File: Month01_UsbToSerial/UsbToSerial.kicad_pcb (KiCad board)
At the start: 2 copper layers, 36.8 x 24.1 mm, 14 parts, among them J1 USB_B_Micro, J2 Conn_01x07_Female, J3 Conn_01x07_Female, U1 FT232RL

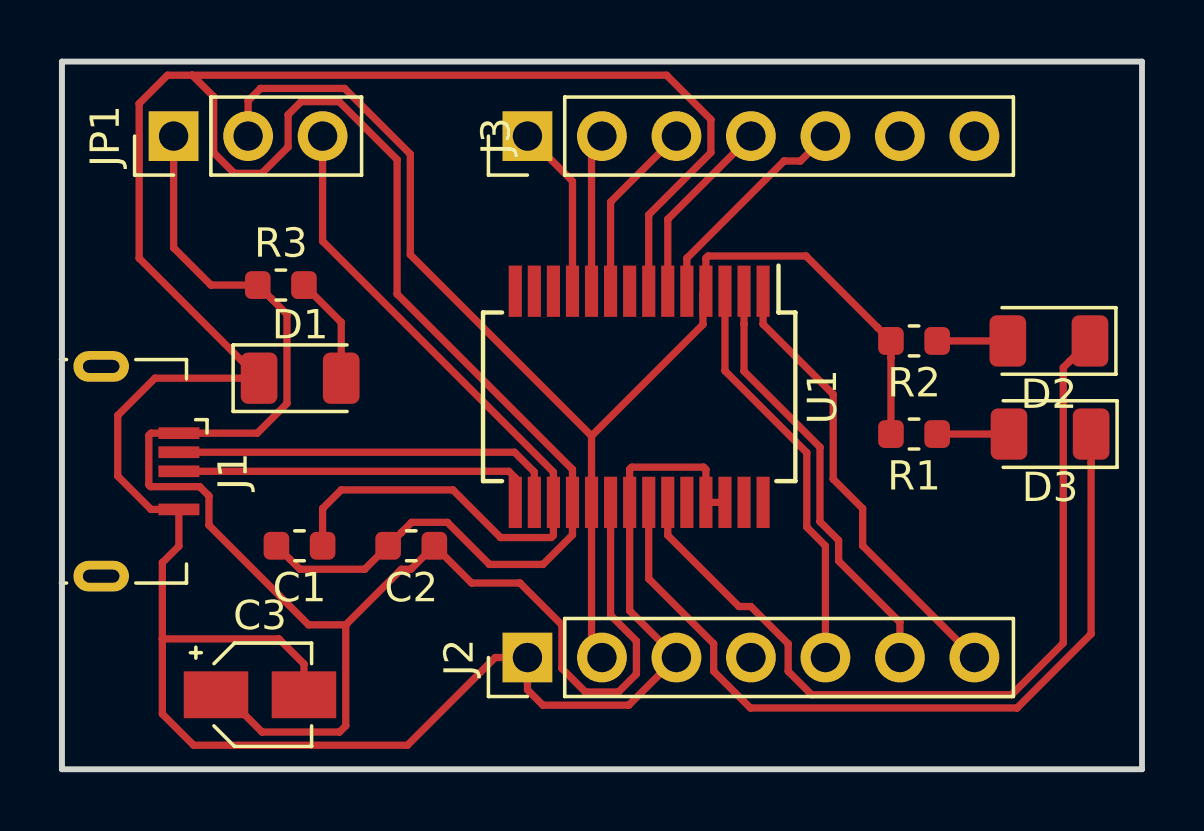
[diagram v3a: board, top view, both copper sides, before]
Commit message: Slight modification to PCB layout, added more to month1 readme
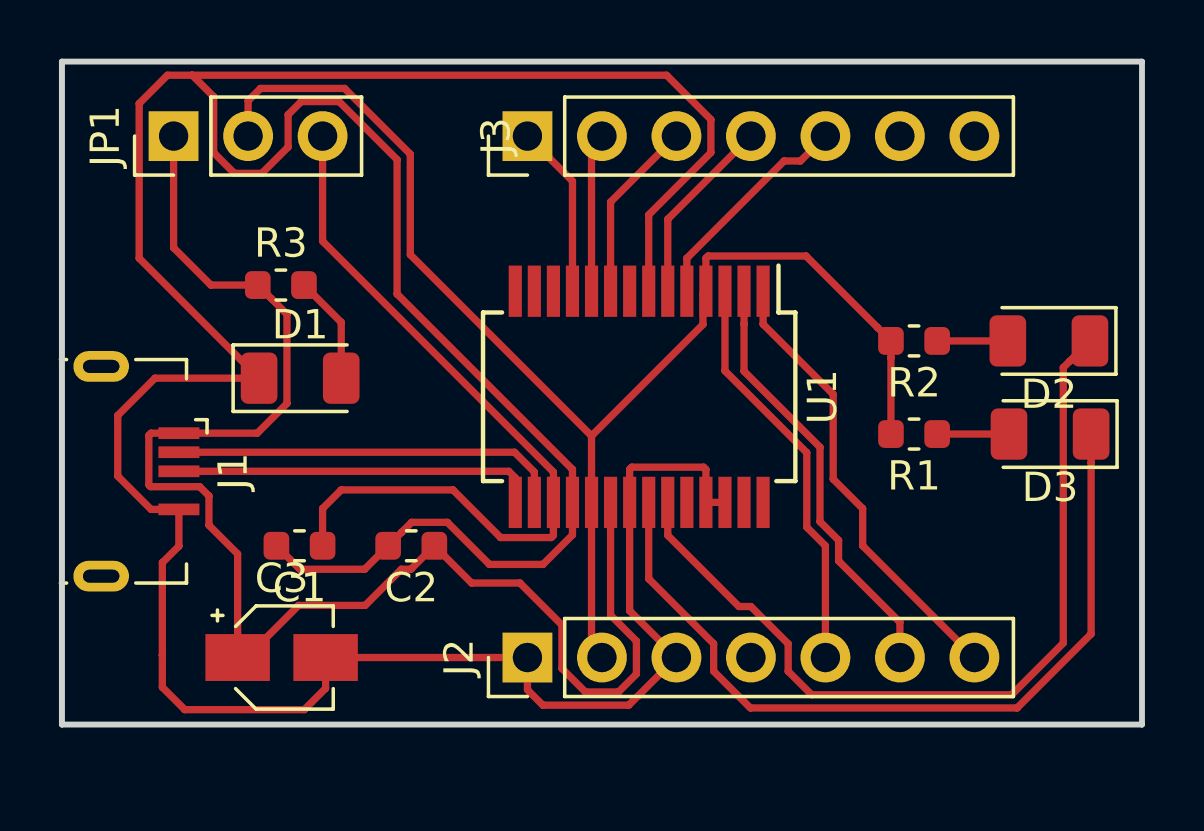
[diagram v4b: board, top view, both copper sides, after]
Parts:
- moved C3 1.47 mm to (84.3, 87.6)
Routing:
- net GNDREF: track 133.8 -> 126.6 mm
- net +5V: track 56.7 -> 51.2 mm
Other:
- board size 36.8 x 24.1 mm -> 36.8 x 22.6 mm
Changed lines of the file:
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@@
-(kicad_pcb (version 20171130) (host pcbnew "(5.0.1)-3")
+(kicad_pcb (version 20171130) (host pcbnew "(5.1.2)-2")
   (general
     (thickness 1.6)
     (drawings 4)
-    (tracks 186)
+    (tracks 184)
     (zones 0)
     (modules 14)
@@
     (zone_45_only no)
     (trace_min 0.2)
-    (segment_width 0.2)
-    (edge_width 0.15)
     (via_size 0.8)
     (via_drill 0.4)
@@
     (uvia_min_size 0.2)
     (uvia_min_drill 0.1)
+    (edge_width 0.15)
+    (segment_width 0.2)
     (pcb_text_width 0.3)
     (pcb_text_size 1.5 1.5)
@@
   )
   (module Capacitor_SMD:CP_Elec_3x5.3 (layer F.Cu)
-    (at 83.59 88.9)
+    (at 84.328 87.63)
     (descr "SMT capacitor, aluminium electrolytic, 3x5.3, Cornell Dubilier Electronics ")
     (tags "Capacitor Electrolytic")
@@
     )
   )
-  (gr_line (start 76.835 91.44) (end 76.835 67.31) (layer Edge.Cuts) (width 0.2))
-  (gr_line (start 113.665 91.44) (end 76.835 91.44) (layer Edge.Cuts) (width 0.2))
-  (gr_line (start 113.665 67.31) (end 113.665 91.44) (layer Edge.Cuts) (width 0.2))
+  (gr_line (start 76.835 89.916) (end 76.835 67.31) (layer Edge.Cuts) (width 0.2))
+  (gr_line (start 113.665 89.916) (end 76.835 89.916) (layer Edge.Cuts) (width 0.2))
+  (gr_line (start 113.665 67.31) (end 113.665 89.916) (layer Edge.Cuts) (width 0.2))
   (gr_line (start 76.835 67.31) (end 113.665 67.31) (layer Edge.Cuts) (width 0.2))
   (segment (start 83.976612 75.391612) (end 83.515 74.93) (width 0.25) (layer F.Cu) (net 1))
@@
   (segment (start 90.805 85.09) (end 89.535 83.82) (width 0.25) (layer F.Cu) (net 1))
   (segment (start 92.455002 85.09) (end 90.805 85.09) (width 0.25) (layer F.Cu) (net 1))
-  (segment (start 82.39 88.9) (end 83.66 90.17) (width 0.25) (layer F.Cu) (net 1))
-  (segment (start 82.09 88.9) (end 82.39 88.9) (width 0.25) (layer F.Cu) (net 1))
-  (segment (start 86.515001 89.960001) (end 86.515001 86.515001) (width 0.25) (layer F.Cu) (net 1))
-  (segment (start 83.66 90.17) (end 86.305002 90.17) (width 0.25) (layer F.Cu) (net 1))
-  (segment (start 86.305002 90.17) (end 86.515001 89.960001) (width 0.25) (layer F.Cu) (net 1))
   (segment (start 79.875 79.98) (end 80.825 79.98) (width 0.25) (layer F.Cu) (net 1))
   (segment (start 79.799999 80.055001) (end 79.875 79.98) (width 0.25) (layer F.Cu) (net 1))
@@
   (segment (start 81.850001 82.119999) (end 81.535003 81.805001) (width 0.25) (layer F.Cu) (net 1))
   (segment (start 81.850001 83.120001) (end 81.850001 82.119999) (width 0.25) (layer F.Cu) (net 1))
-  (segment (start 85.245001 86.515001) (end 81.850001 83.120001) (width 0.25) (layer F.Cu) (net 1))
-  (segment (start 86.515001 86.515001) (end 85.245001 86.515001) (width 0.25) (layer F.Cu) (net 1))
-  (segment (start 88.409992 84.62001) (end 86.515001 86.515001) (width 0.25) (layer F.Cu) (net 1))
   (segment (start 88.73499 84.62001) (end 88.409992 84.62001) (width 0.25) (layer F.Cu) (net 1))
   (segment (start 89.535 83.82) (end 88.73499 84.62001) (width 0.25) (layer F.Cu) (net 1))
-  (segment (start 80.825 83.832095) (end 80.259999 84.397096) (width 0.25) (layer F.Cu) (net 2))
-  (segment (start 80.825 82.58) (end 80.825 83.832095) (width 0.25) (layer F.Cu) (net 2))
+  (segment (start 83.128 87.63) (end 82.828 87.63) (width 0.25) (layer F.Cu) (net 1))
+  (segment (start 84.906 85.852) (end 83.128 87.63) (width 0.25) (layer F.Cu) (net 1))
+  (segment (start 87.178002 85.852) (end 84.906 85.852) (width 0.25) (layer F.Cu) (net 1))
+  (segment (start 88.409992 84.62001) (end 87.178002 85.852) (width 0.25) (layer F.Cu) (net 1))
+  (segment (start 82.828 84.098) (end 81.850001 83.120001) (width 0.25) (layer F.Cu) (net 1))
+  (segment (start 82.828 87.63) (end 82.828 84.098) (width 0.25) (layer F.Cu) (net 1))
   (segment (start 83.56 78.105) (end 80.01 78.105) (width 0.25) (layer F.Cu) (net 2))
   (segment (start 80.01 78.105) (end 78.74 79.375) (width 0.25) (layer F.Cu) (net 2))
@@
   (segment (start 96.195 81.215) (end 96.270001 81.139999) (width 0.25) (layer F.Cu) (net 2))
   (segment (start 96.195 82.34) (end 96.195 81.215) (width 0.25) (layer F.Cu) (net 2))
-  (segment (start 85.09 87.85) (end 84.235 86.995) (width 0.25) (layer F.Cu) (net 2))
-  (segment (start 85.09 88.9) (end 85.09 87.85) (width 0.25) (layer F.Cu) (net 2))
-  (segment (start 84.235 86.995) (end 80.259999 86.995) (width 0.25) (layer F.Cu) (net 2))
-  (segment (start 80.259999 84.397096) (end 80.259999 85.09) (width 0.25) (layer F.Cu) (net 2))
-  (segment (start 80.259999 85.09) (end 80.259999 86.995) (width 0.25) (layer F.Cu) (net 2))
   (segment (start 79.469999 68.739999) (end 79.469999 74.014999) (width 0.25) (layer F.Cu) (net 2))
   (segment (start 96.845 72.534002) (end 98.965001 70.414001) (width 0.25) (layer F.Cu) (net 2))
@@
   (segment (start 96.16499 89.25501) (end 93.23501 89.25501) (width 0.25) (layer F.Cu) (net 2))
   (segment (start 97.79 87.63) (end 96.16499 89.25501) (width 0.25) (layer F.Cu) (net 2))
-  (segment (start 80.259999 89.555001) (end 80.259999 86.995) (width 0.25) (layer F.Cu) (net 2))
-  (segment (start 81.325007 90.620009) (end 80.259999 89.555001) (width 0.25) (layer F.Cu) (net 2))
-  (segment (start 88.619991 90.620009) (end 81.325007 90.620009) (width 0.25) (layer F.Cu) (net 2))
-  (segment (start 91.61 87.63) (end 88.619991 90.620009) (width 0.25) (layer F.Cu) (net 2))
   (segment (start 92.71 87.63) (end 91.61 87.63) (width 0.25) (layer F.Cu) (net 2))
+  (segment (start 91.61 87.63) (end 85.828 87.63) (width 0.25) (layer F.Cu) (net 2))
+  (segment (start 80.825 83.832095) (end 80.259999 84.397096) (width 0.25) (layer F.Cu) (net 2))
+  (segment (start 80.825 82.58) (end 80.825 83.832095) (width 0.25) (layer F.Cu) (net 2))
+  (segment (start 80.259999 84.397096) (end 80.259999 85.09) (width 0.25) (layer F.Cu) (net 2))
+  (segment (start 80.259999 85.09) (end 80.259999 87.547001) (width 0.25) (layer F.Cu) (net 2))
+  (segment (start 80.259999 87.547001) (end 80.264 87.551002) (width 0.25) (layer F.Cu) (net 2))
+  (segment (start 85.828 88.68) (end 85.828 87.63) (width 0.25) (layer F.Cu) (net 2))
+  (segment (start 85.1 89.408) (end 85.828 88.68) (width 0.25) (layer F.Cu) (net 2))
+  (segment (start 81.026 89.408) (end 85.1 89.408) (width 0.25) (layer F.Cu) (net 2))
+  (segment (start 80.259999 88.641999) (end 81.026 89.408) (width 0.25) (layer F.Cu) (net 2))
+  (segment (start 80.259999 87.547001) (end 80.259999 88.641999) (width 0.25) (layer F.Cu) (net 2))
   (segment (start 109.09 76.835) (end 106.68 76.835) (width 0.25) (layer F.Cu) (net 3))
   (segment (start 111.19429 77.53071) (end 111.89 76.835) (width 0.25) (layer F.Cu) (net 4))

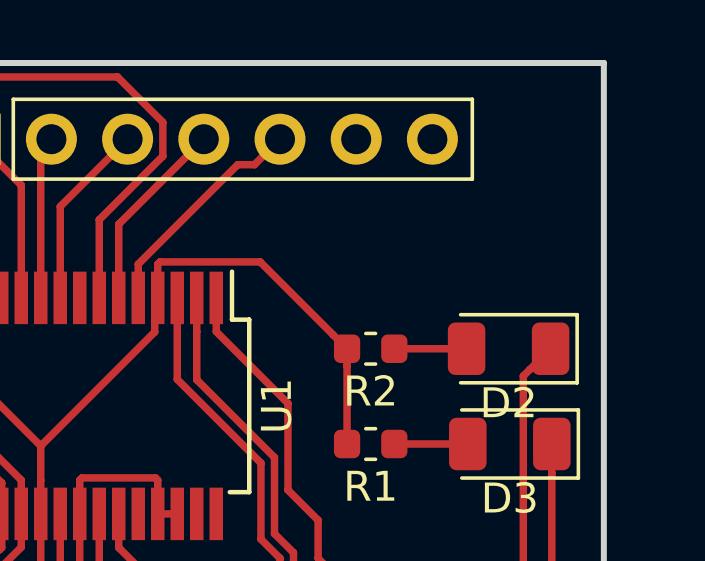
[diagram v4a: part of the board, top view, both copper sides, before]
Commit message: Added version number to board
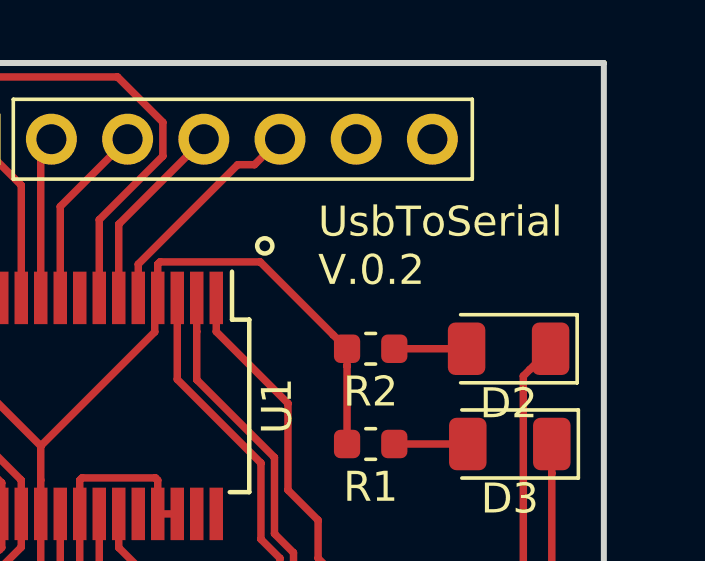
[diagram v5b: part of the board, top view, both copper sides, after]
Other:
- board text added: "UsbToSerial V.0.2"
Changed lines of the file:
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@@
   (general
     (thickness 1.6)
-    (drawings 4)
+    (drawings 7)
     (tracks 184)
     (zones 0)
@@
     (47 F.CrtYd user)
     (48 B.Fab user)
-    (49 F.Fab user)
+    (49 F.Fab user hide)
   )
   (setup
@@
     )
   )
+  (gr_circle (center 102.362 73.406) (end 102.616 73.406) (layer F.SilkS) (width 0.15))
+  (gr_circle (center 101.092 73.152) (end 101.346 73.406) (layer F.Fab) (width 0.15))
+  (gr_text "UsbToSerial\nV.0.2" (at 104.14 73.406) (layer F.SilkS)
+    (effects (font (size 1 1) (thickness 0.15)) (justify left))
+  )
   (gr_line (start 76.835 89.916) (end 76.835 67.31) (layer Edge.Cuts) (width 0.2))
